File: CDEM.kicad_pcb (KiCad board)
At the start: 2 copper layers, 80.7 x 51.5 mm, 42 parts, among them J1 USB_C_Receptacle_USB2.0, J2 6P6C, J3 Conn_01x04, Q1 2N7002, Q2 S8050, Q3 S8050, SW1 BTN, SW2 RESET, U1 AMS1117-3.3, U2 USBLC6-2SC6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

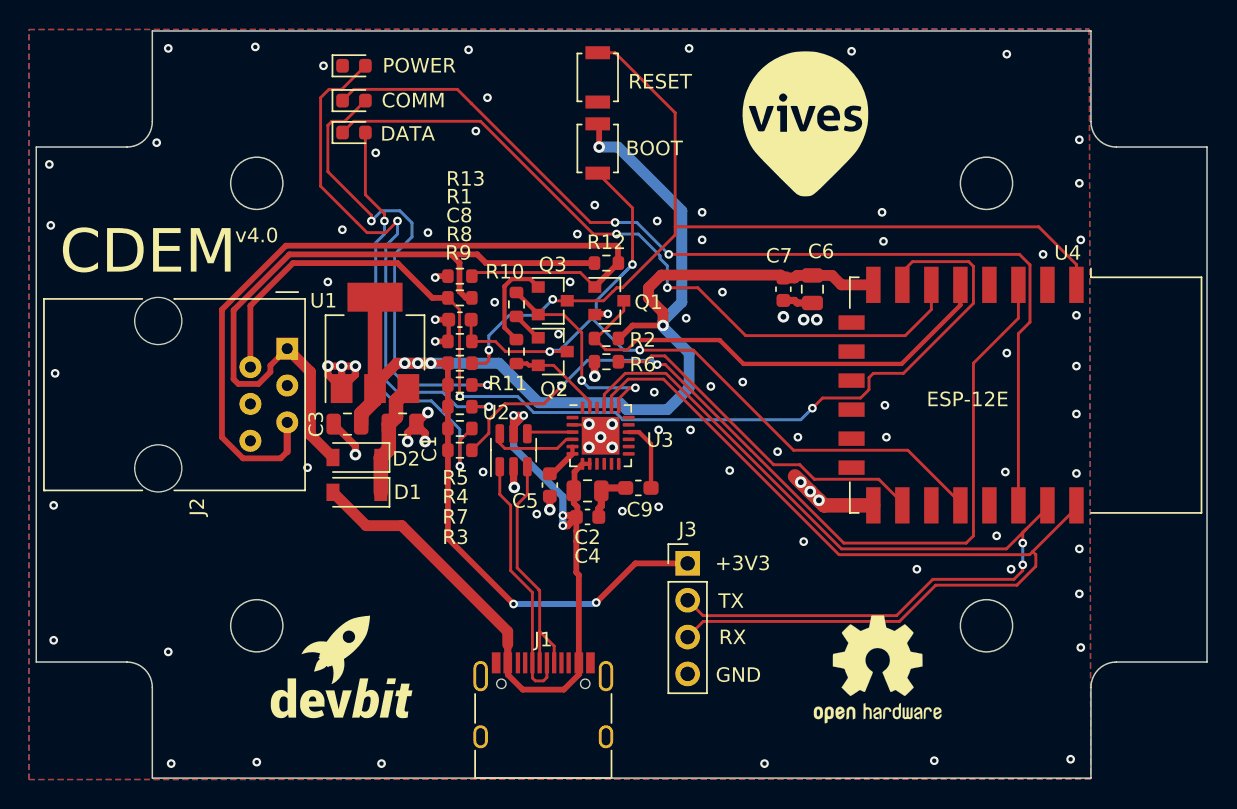
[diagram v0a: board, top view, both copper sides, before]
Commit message: Replace LDO and diodes with better alternatives. Also add programming jumper
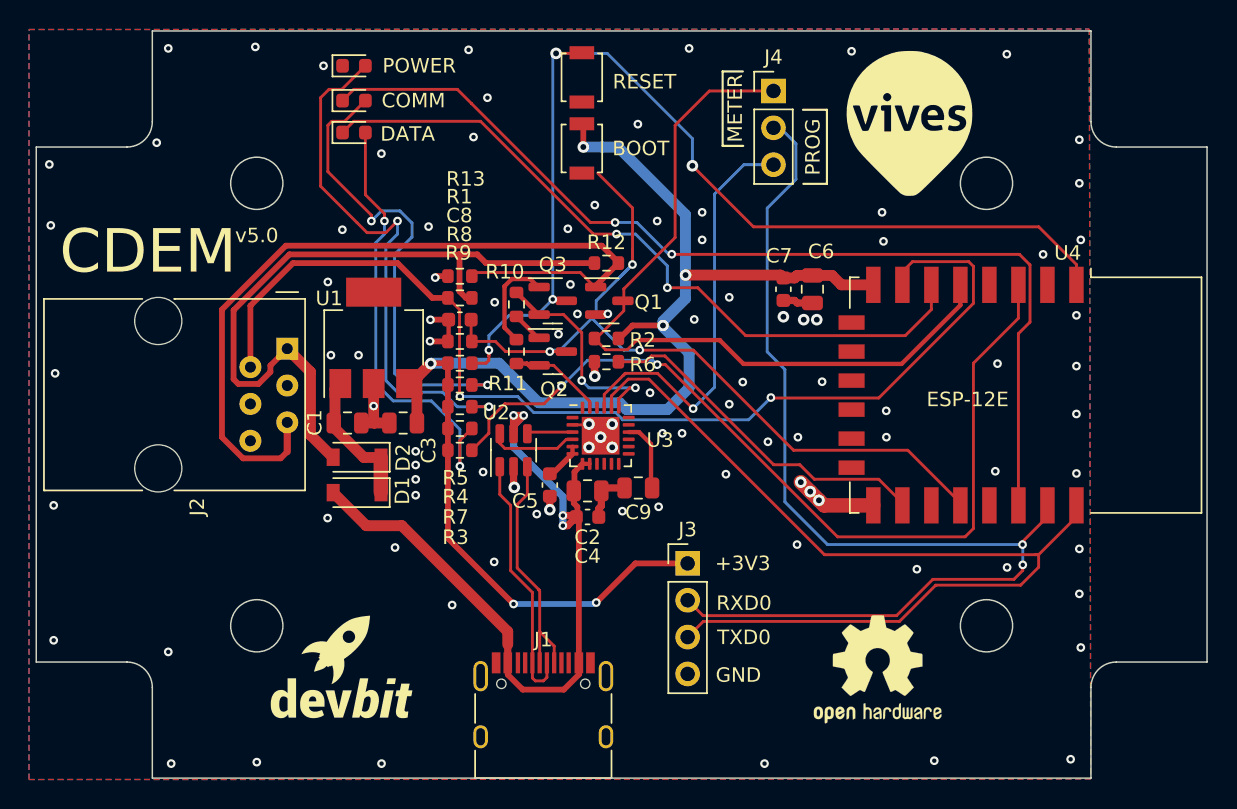
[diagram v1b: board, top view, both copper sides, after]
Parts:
- added J4: Conn_01x03, Connector_PinHeader_2.54mm:PinHeader_1x03_P2.54mm_Vertical, F.Cu at (77.2, 84.8)
- C9: footprint Capacitor_SMD:C_0603_1608Metric_Pad1.05x0.95mm_HandSolder -> Capacitor_SMD:C_0805_2012Metric
- D1, D2: value 1N4148W -> 1N5817
- U1: value AMS1117-3.3 -> MCP1825S
- moved L2 7.17 mm to (86.7, 87.0)
- moved C3 3.84 mm to (51.7, 107.7)
- moved C1 3.80 mm to (47.9, 107.7)
- moved SW1 1.09 mm to (64.0, 88.8)
- moved SW2 1.09 mm to (64.0, 83.9)
- moved U1 0.36 mm to (49.7, 101.9)
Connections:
- J1 pad A5: Net-(J1-PadA5) -> unconnected-(J1-PadA5)
- J1 pad A8: Net-(J1-PadA8) -> unconnected-(J1-PadA8)
- J1 pad B5: Net-(J1-PadB5) -> unconnected-(J1-PadB5)
- J1 pad B8: Net-(J1-PadB8) -> unconnected-(J1-PadB8)
- J2 pad 4: Net-(J2-Pad4) -> unconnected-(J2-Pad4)
- J2 pad 5: /SM-DATA -> /SM-DATA-ORIGINAL
- J3 pad 2: /USB-TX -> /SM-USB-TX
- Q1 pad 1: /SM-DATA -> /SM-DATA-ORIGINAL
- Q1 pad 3: /DATA -> /SM-DATA
- R12 pad 2: /SM-DATA -> /SM-DATA-ORIGINAL
- R13 pad 1: /SM-DATA -> /SM-DATA-ORIGINAL
- R2 pad 2: /DATA -> /SM-DATA
- U1 pad 1: GND -> Net-(C1-Pad1)
- U1 pad 2: +3V3 -> GND
- U1 pad 3: Net-(C1-Pad1) -> +3V3
- U3 pad 1: Net-(U3-Pad1) -> unconnected-(U3-Pad1)
- U3 pad 10: no_connect_56 -> unconnected-(U3-Pad10)
- U3 pad 11: Net-(U3-Pad11) -> unconnected-(U3-Pad11)
- U3 pad 12: Net-(U3-Pad12) -> unconnected-(U3-Pad12)
- U3 pad 13: Net-(U3-Pad13) -> unconnected-(U3-Pad13)
- U3 pad 14: Net-(U3-Pad14) -> unconnected-(U3-Pad14)
- U3 pad 15: Net-(U3-Pad15) -> unconnected-(U3-Pad15)
- U3 pad 17: Net-(U3-Pad17) -> unconnected-(U3-Pad17)
- U3 pad 18: Net-(U3-Pad18) -> unconnected-(U3-Pad18)
- U3 pad 22: Net-(U3-Pad22) -> unconnected-(U3-Pad22)
- U3 pad 24: Net-(U3-Pad24) -> unconnected-(U3-Pad24)
- U3 pad 9: Net-(U3-Pad9) -> unconnected-(U3-Pad9)
- U4 pad 10: Net-(U4-Pad10) -> unconnected-(U4-Pad10)
- U4 pad 11: Net-(U4-Pad11) -> unconnected-(U4-Pad11)
- U4 pad 12: Net-(U4-Pad12) -> unconnected-(U4-Pad12)
- U4 pad 13: Net-(U4-Pad13) -> unconnected-(U4-Pad13)
- U4 pad 14: Net-(U4-Pad14) -> unconnected-(U4-Pad14)
- U4 pad 17: /SM-TX -> unconnected-(U4-Pad17)
- U4 pad 19: Net-(U4-Pad19) -> unconnected-(U4-Pad19)
- U4 pad 2: Net-(U4-Pad2) -> unconnected-(U4-Pad2)
- U4 pad 21: /USB-TX -> /SM-USB-TX
- U4 pad 4: Net-(U4-Pad4) -> unconnected-(U4-Pad4)
- U4 pad 5: /DATA -> unconnected-(U4-Pad5)
- U4 pad 9: Net-(U4-Pad9) -> unconnected-(U4-Pad9)
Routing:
- net /SM-USB-TX: track 0.00 -> 75.7 mm, vias 0 -> 2
- net /SM-DATA-ORIGINAL: track 0.00 -> 57.1 mm
- net /USB-TX: track 66.2 -> 29.2 mm, vias 2 -> 1
- net /DATA: track 33.1 -> 0.00 mm
- net +3V3: track 118.4 -> 99.0 mm, vias 7 -> 6
- net GND: track 35.9 -> 27.0 mm, vias 95 -> 100
- net /RESET: track 64.6 -> 72.9 mm, vias 2 -> 4
- net /SM-DATA: track 57.7 -> 54.5 mm
- net Net-(C1-Pad1): track 7.94 -> 9.71 mm
- net Net-(R3-Pad2): track 61.7 -> 61.0 mm
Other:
- board text added: "METER"
- board text added: "PROG"
- board text added: "RXD0"
- board text added: "TXD0"
- board text added: "v5.0"
- board text removed: "RX"
- board text removed: "TX"
- board text removed: "v4.0"
